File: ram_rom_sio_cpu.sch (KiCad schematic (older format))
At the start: 17 parts, among them J4 Port A, U1 SST39LF040, U2 Z84C0010AEG, U3 AS6C4008A-55ZIN, U4 Z84C4310AEG

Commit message: reorganized SIO
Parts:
- removed RN2: 2K2, Resistor_SMD:R_Cat16-4, symbol Device:R_Pack04
- added R3, R4, R5, R6: 2K2, Resistor_SMD:R_0603_1608Metric_Pad1.05x0.95mm_HandSolder, symbol Device:R_Small
- U4: renamed from U3; symbol SMC-80-rescue:AS6C4008A-55ZIN-Memory_RAM -> SMC-80_DE10-rescue:AS6C4008A-55ZIN-Memory_RAM-SMC-80-rescue
- renumbered R4 to R10, R6 to R11, R10 to R12, R5 to R2, U2 to U1, U4 to U2, U1 to U3

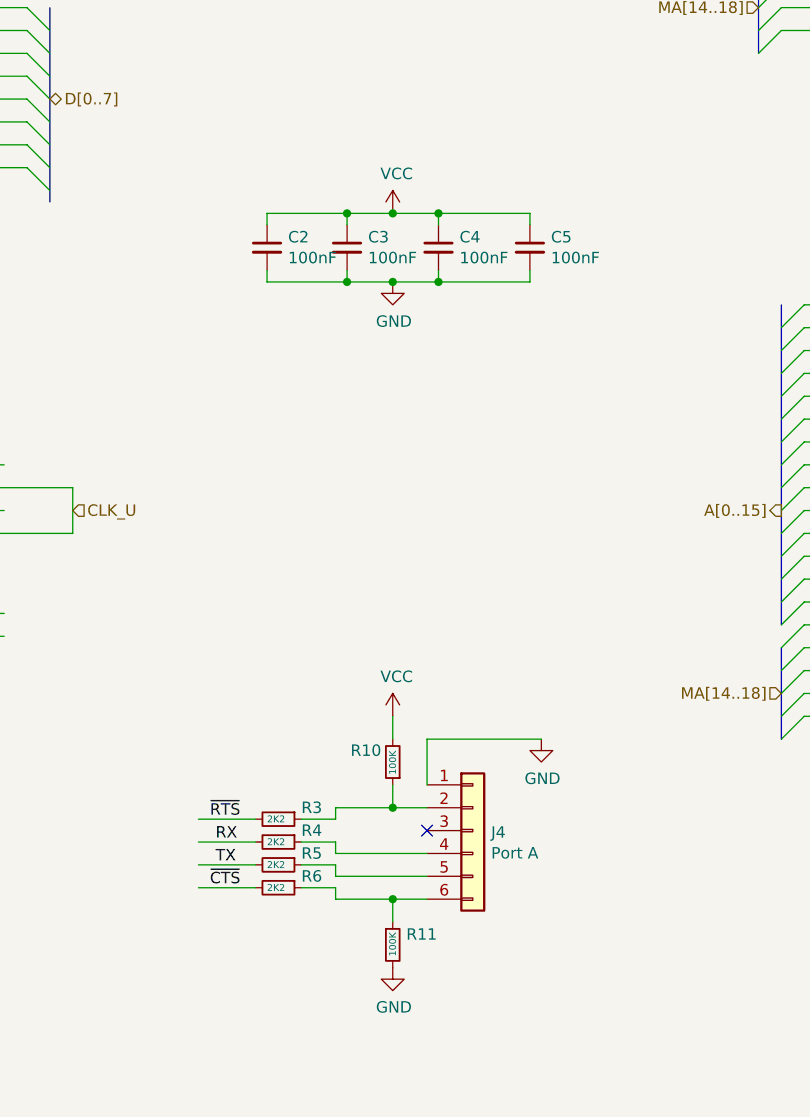
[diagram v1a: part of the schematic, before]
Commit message: reorganized schematic, added missing pin label
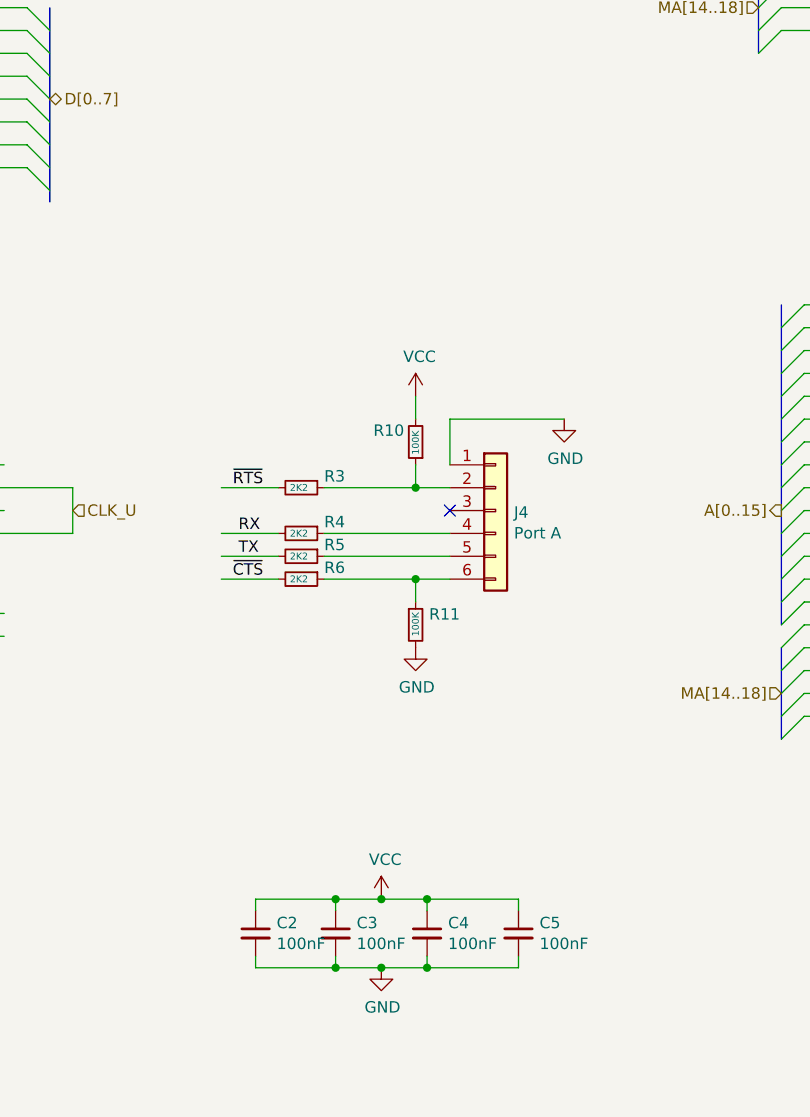
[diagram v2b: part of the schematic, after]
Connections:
- wire segments 178 -> 170
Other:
- moved on the sheet: C2, C3, C4, C5, J4, R10, R11, R3, R4, R5, R6

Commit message: added SIO port B clock
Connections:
- wire segments 170 -> 173
- no-connect marks 16 -> 14
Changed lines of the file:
@@
 NoConn ~ 3600 6750
 NoConn ~ 3600 6650
-NoConn ~ 3600 6300
 NoConn ~ 3600 6200
-NoConn ~ 3600 6100
 NoConn ~ 3600 6000
 Wire Wire Line
@@
 Wire Wire Line
 	5550 5100 6100 5100
+Wire Wire Line
+	4450 6100 4450 6300
+Wire Wire Line
+	3600 6100 4450 6100
+Wire Wire Line
+	3600 6300 4450 6300
+Text HLabel 4450 6200 2    50   Input ~ 0
+CLK_U
 Wire Bus Line
 	1550 5700 1550 5850

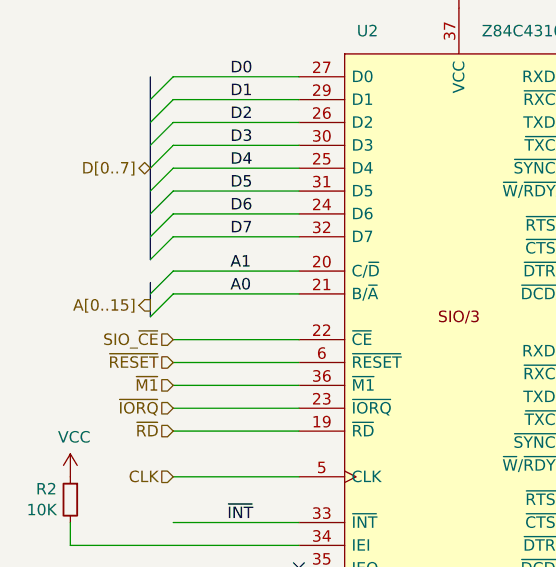
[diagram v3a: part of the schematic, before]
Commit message: Broke out SIO C/D and B/A pins
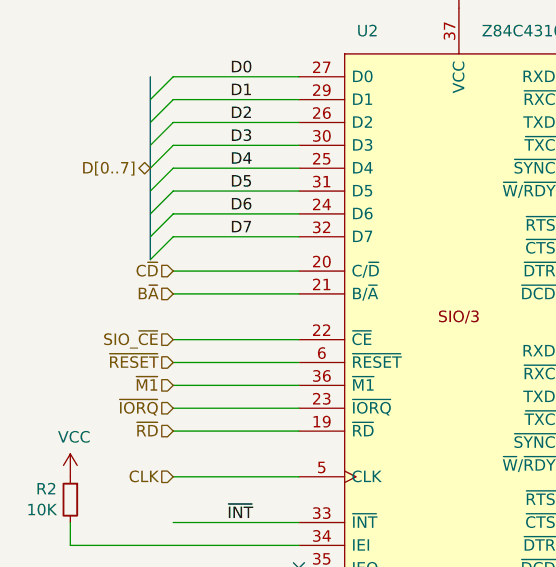
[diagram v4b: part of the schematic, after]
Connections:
- net labels added: B~A, C~D
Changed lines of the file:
@@
 Wire Wire Line
 	2200 5750 1650 5750
-Text Label 1900 5750 0    50   ~ 0
-A0
-Text Label 1900 5650 0    50   ~ 0
-A1
-Entry Wire Line
-	1650 5650 1550 5750
-Entry Wire Line
-	1650 5750 1550 5850
 Wire Wire Line
 	2200 5950 1650 5950
@@
 Text Label 2000 6750 2    50   ~ 0
 ~INT
-Text HLabel 1550 5800 0    50   Output ~ 0
-A[0..15]
 Text HLabel 1650 6050 0    50   Input ~ 0
 ~RESET
@@
 Text HLabel 4450 6200 2    50   Input ~ 0
 CLK_U
-Wire Bus Line
-	1550 5700 1550 5850
+Text HLabel 1650 5750 0    50   Input ~ 0
+B~A
 Wire Bus Line
 	7550 5600 7550 6000
 Wire Bus Line
+	7550 4100 7550 5500
+Wire Bus Line
+	1550 4800 1550 5600
+Wire Bus Line
 	7450 2600 7450 3000
 Wire Bus Line
-	1550 4800 1550 5600
+	7450 1100 7450 2500
 Wire Bus Line
 	9850 4100 9850 4950
@@
 	4350 2800 4350 3650
 Wire Bus Line
-	7450 1100 7450 2500
-Wire Bus Line
-	7550 4100 7550 5500
-Wire Bus Line
 	4350 1100 4350 2700
+Text HLabel 1650 5650 0    50   Input ~ 0
+C~D
 $EndSCHEMATC
